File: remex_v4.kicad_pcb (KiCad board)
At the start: 4 copper layers, 38 x 35 mm, 22 parts, among them J1 Conn_01x03_Male, J10 Conn_01x04_Male, J11 Conn_01x04_Male, J2 Conn_01x03_Male, J3 Conn_01x06_Male, J4 Conn_01x04_Male, J5 Conn_01x02_Male, J6 Conn_01x03_Male, J7 Conn_01x02_Male, J8 Conn_01x03_Male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

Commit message: added qr to link to the repo
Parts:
- added G***: LOGO, LOGO, B.Cu at (203.2, 107.7)

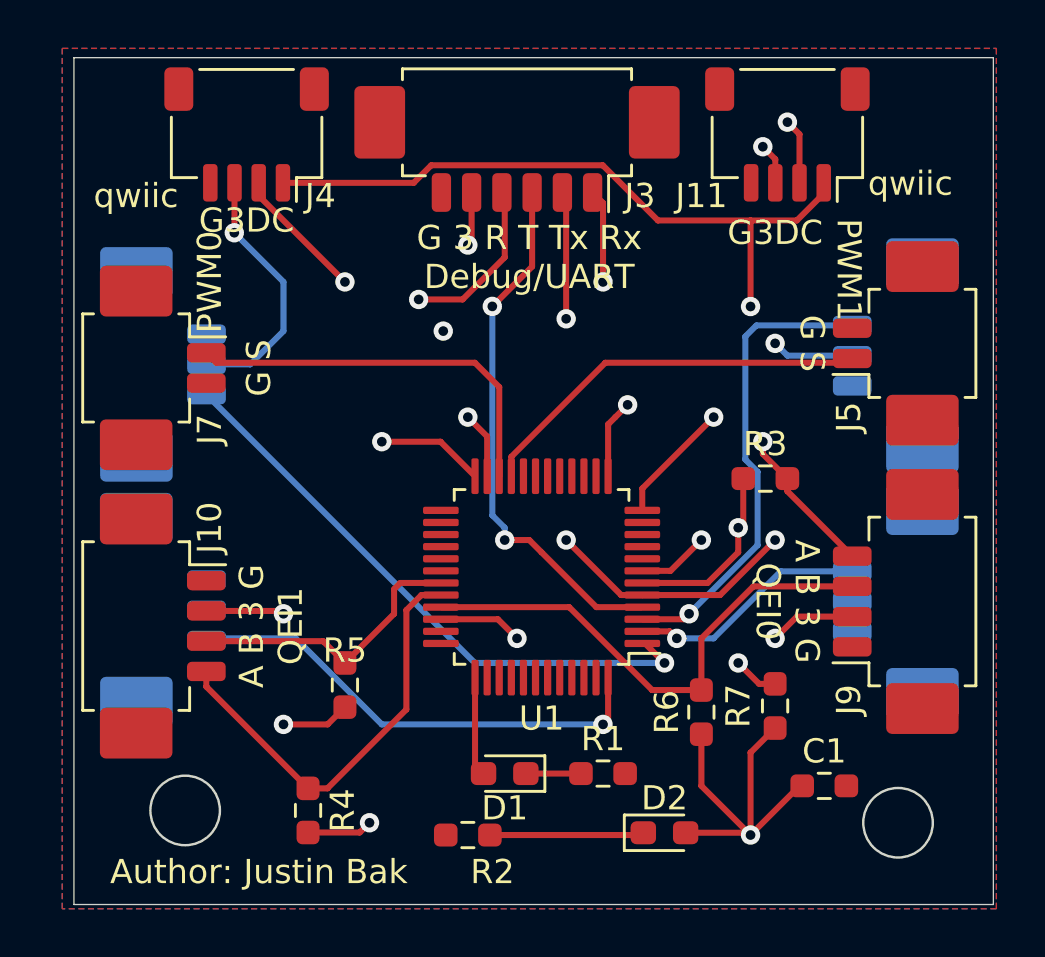
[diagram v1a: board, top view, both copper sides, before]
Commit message: Corrected qwiic orientation, added silkscreen details, changed diodes to 0805, fixed bugs with qei
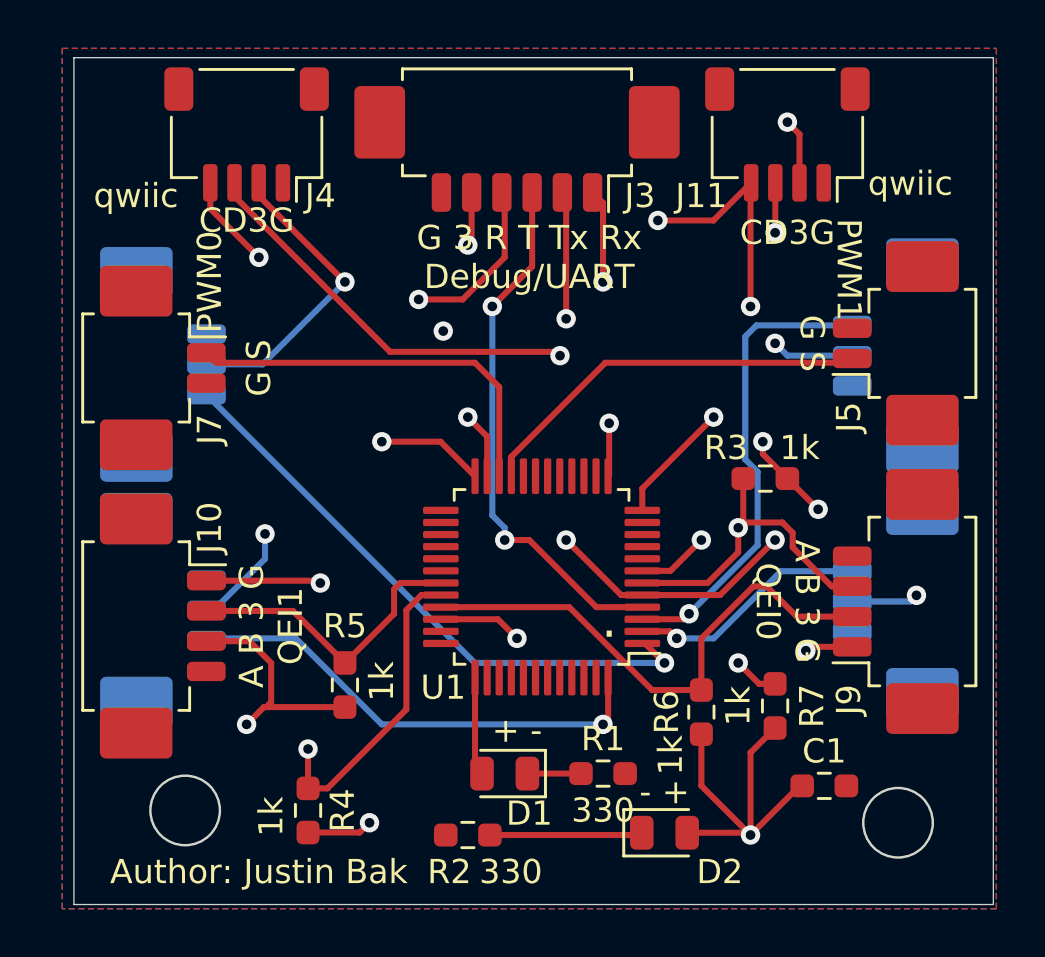
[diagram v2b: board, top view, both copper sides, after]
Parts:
- D1, D2: footprint LED_SMD:LED_0603_1608Metric_Pad1.05x0.95mm_HandSolder -> LED_SMD:LED_0805_2012Metric
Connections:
- J11 pad 1: /SCL -> GND
- J11 pad 2: /SDA -> +3.3V
- J11 pad 3: +3.3V -> /SDA
- J11 pad 4: GND -> /SCL
- J4 pad 1: /SCL -> GND
- J4 pad 2: /SDA -> +3.3V
- J4 pad 3: +3.3V -> /SDA
- J4 pad 4: GND -> /SCL
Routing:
- net +3.3V: track 47.3 -> 103.3 mm, vias 8 -> 11
- net /SDA: track 45.3 -> 35.4 mm, vias 4 -> 3
- net Net-(J10-Pad1): track 17.8 -> 24.7 mm, vias 0 -> 2
- net Net-(J9-Pad1): track 23.3 -> 28.8 mm, vias 2 -> 4
- net Net-(J9-Pad2): track 25.0 -> 22.0 mm, vias 1 -> 0
- net Net-(J10-Pad2): track 15.3 -> 12.5 mm, vias 1 -> 0
- net /SCL: track 38.3 -> 40.9 mm, vias 2 -> 4
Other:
- board text added: "+ -"
- board text added: "- +"
- board text added: "."
- board text added: "1k"
- board text added: "330"
- board text added: "CD3G"
- board text added: "S3G"
- board text removed: "G3DC"

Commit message: silkscreen typo
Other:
- board text added: "G 3 A B QEI0"
- board text added: "G 3 A B QEI1"
- board text removed: "A B 3 G QEI0"
- board text removed: "A B 3 G QEI1"
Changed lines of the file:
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@@
     (effects (font (size 1 1) (thickness 0.15)))
   )
-  (gr_text "A B 3 G\nQEI1" (at 200.152 126.492 90) (layer "F.SilkS")
+  (gr_text "G 3 A B\nQEI1" (at 200.152 126.492 90) (layer "F.SilkS")
     (effects (font (size 1 1) (thickness 0.15)))
   )
@@
     (effects (font (size 1 1) (thickness 0.15)))
   )
-  (gr_text "A B 3 G\nQEI0" (at 221.488 125.476 270) (layer "F.SilkS")
+  (gr_text "G 3 A B\nQEI0" (at 221.488 125.476 270) (layer "F.SilkS")
     (effects (font (size 1 1) (thickness 0.15)))
   )
